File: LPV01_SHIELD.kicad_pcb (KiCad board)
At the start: 4 copper layers, 88 x 70 mm, 136 parts, among them J1 GPIO_header, J10 Screw_Terminal_01x02, J11 PWR_input, J2 PWR_socket, J3 SPI_header, J4 Wiegand, J5 Conn_01x02_Pin, J6 Wiegand, J8 Inputs, J9 Inputs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

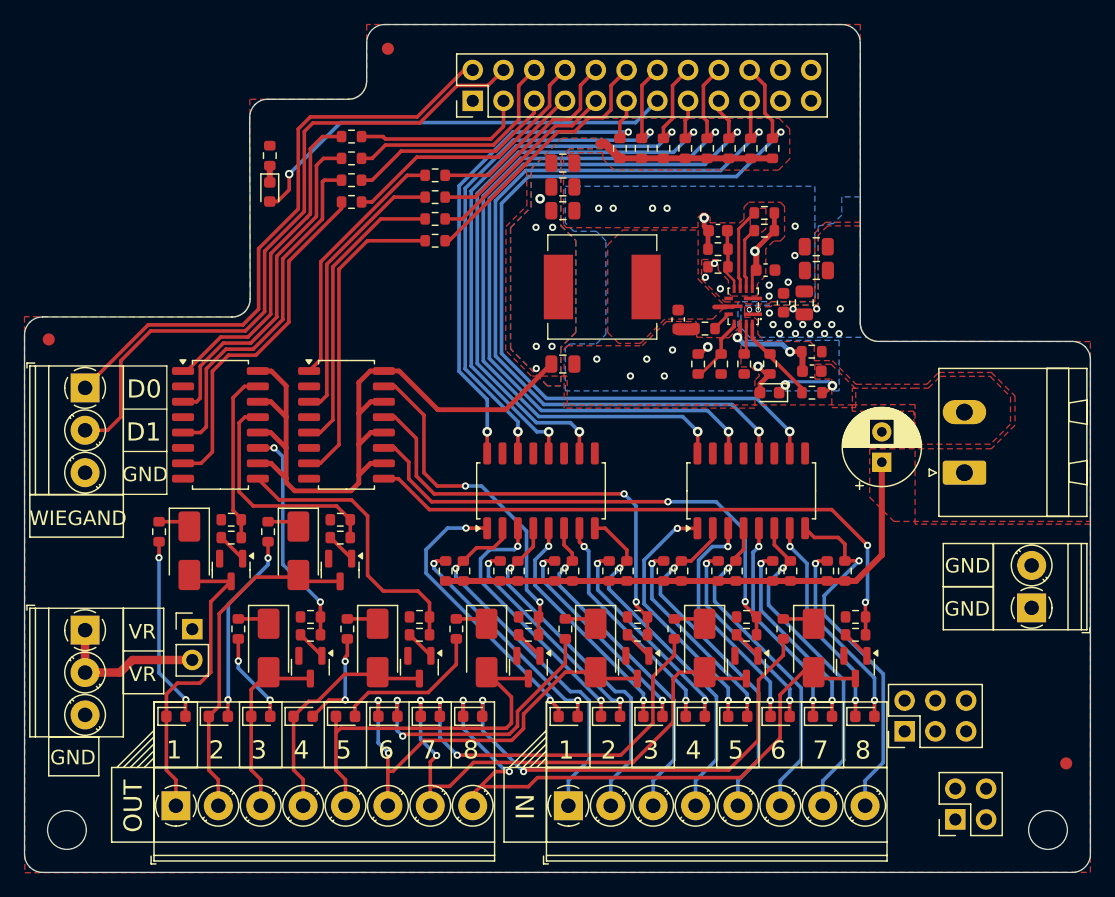
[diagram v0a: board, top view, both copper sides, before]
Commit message: Added fan connector
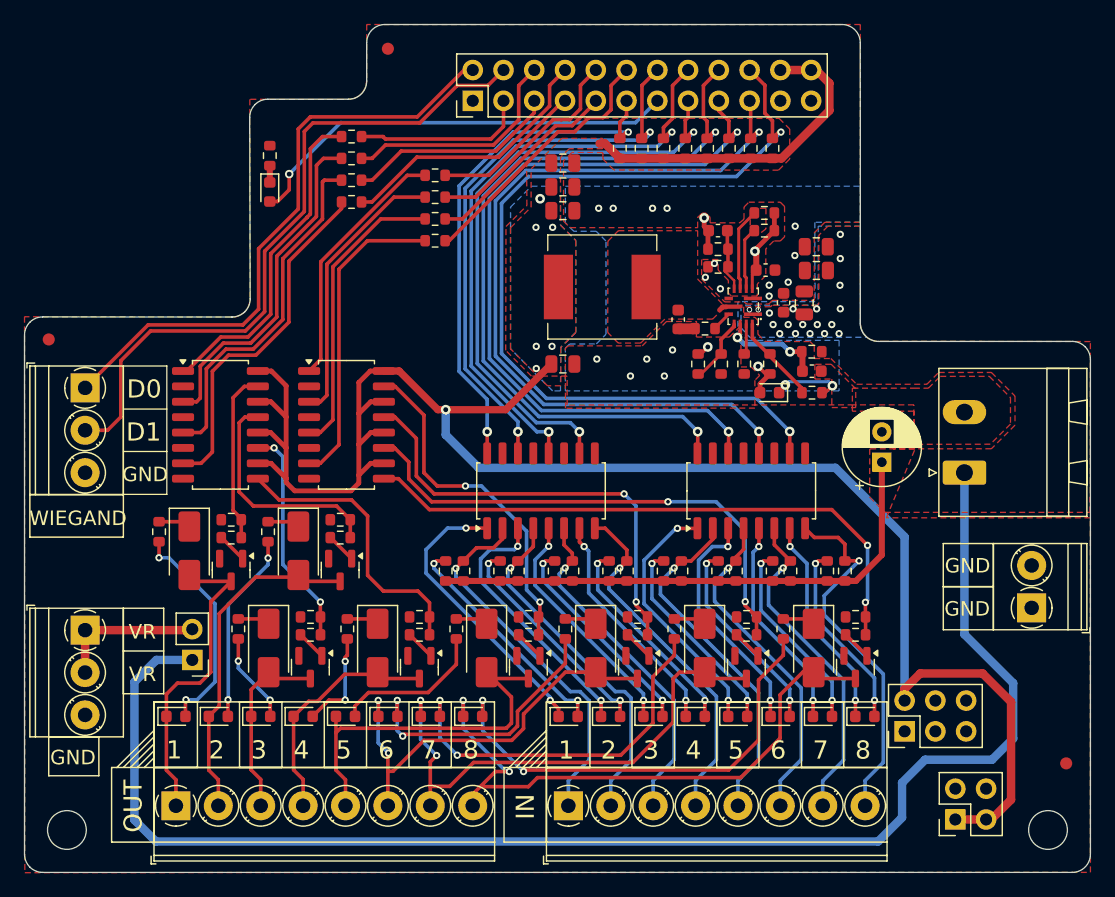
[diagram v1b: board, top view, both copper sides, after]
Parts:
- moved J5 2.54 mm to (63.9, 72.5), turned to 180 degrees
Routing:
- net +24V: track 44.6 -> 163.6 mm, vias 16 -> 19
- net +5V: track 92.6 -> 187.3 mm, vias 7 -> 8
- net Net-(D1-A): track 15.4 -> 18.4 mm

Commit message: Filled all the fields
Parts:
- added J7: Fan, Connector:FanPinHeader_1x03_P2.54mm_Vertical, F.Cu at (79.2, 42.0)
- moved R11 1.41 mm to (59.7, 61.9)
- moved D2 1.00 mm to (62.6, 63.4)
- moved Q1 1.00 mm to (66.1, 65.0)
- moved R10 1.00 mm to (66.1, 62.4)
- moved R9 1.00 mm to (66.1, 60.9)
- moved R14 0.61 mm to (69.5, 61.9)
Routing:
- net VR: track 33.7 -> 134.2 mm, vias 0 -> 5
- net +5V: track 187.3 -> 194.4 mm
- net /O4: track 23.9 -> 23.3 mm
- net /OUT1: track 26.1 -> 25.4 mm
- net Net-(D1-A): track 18.4 -> 19.0 mm
- net GND: vias 17 -> 21

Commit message: Version 1 finished
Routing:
- net GND: vias 21 -> 50
- net +24V: vias 19 -> 22
